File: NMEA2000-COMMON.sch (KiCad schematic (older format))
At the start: 67 parts, among them J2 CAN, Q1 BSS138, Q2 BSS138, SW1 PRG, SW2 INSTANCE, SW3 BUS, U1 MCP2551-I-P, U101 74HC165, U2 TMR-2-2411, U3 74HCT595, U4 74HCT595, U5 Teensy_4.0

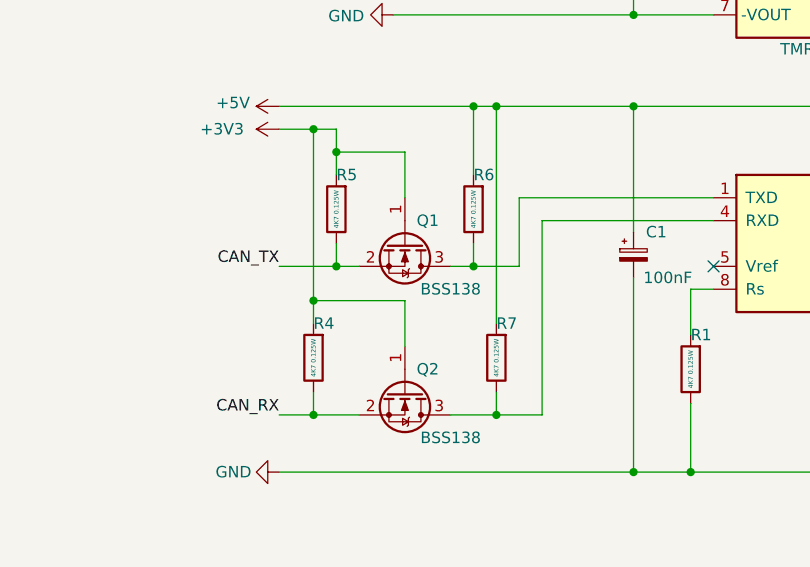
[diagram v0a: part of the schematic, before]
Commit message: Revise logic shifter R values
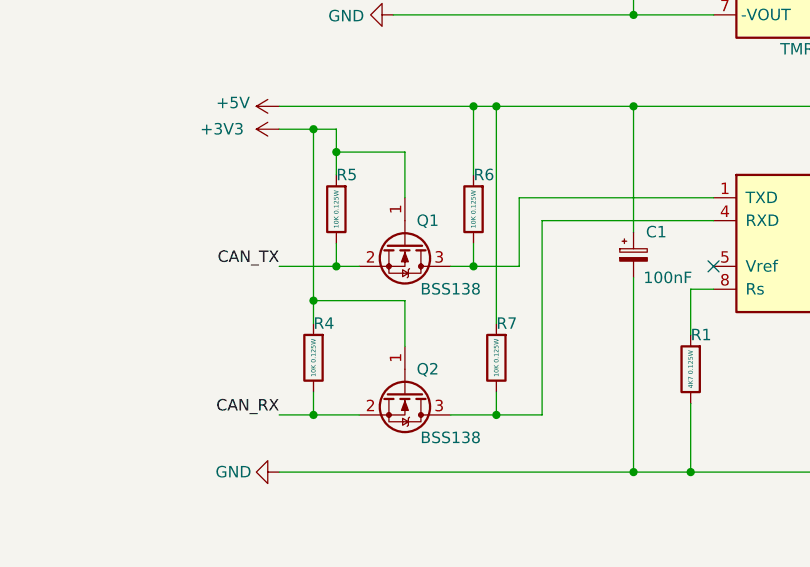
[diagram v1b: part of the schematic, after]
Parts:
- R4, R5, R6, R7: value 4K7 0.125W -> 10K 0.125W
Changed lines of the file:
@@
 P 1500 2200
 F 0 "R5" H 1500 2050 50  0000 R CNN
-F 1 "4K7 0.125W" V 1500 2200 20  0000 C CNN
+F 1 "10K 0.125W" V 1500 2200 20  0000 C CNN
 F 2 "Resistor_SMD:R_0805_2012Metric" V 1430 2200 50  0001 C CNN
 F 3 "~" H 1500 2200 50  0001 C CNN
@@
 P 2100 2200
 F 0 "R6" H 2100 2050 50  0000 R CNN
-F 1 "4K7 0.125W" V 2100 2200 20  0000 C CNN
+F 1 "10K 0.125W" V 2100 2200 20  0000 C CNN
 F 2 "Resistor_SMD:R_0805_2012Metric" V 2030 2200 50  0001 C CNN
 F 3 "~" H 2100 2200 50  0001 C CNN
@@
 P 1400 2850
 F 0 "R4" H 1400 2700 50  0000 R CNN
-F 1 "4K7 0.125W" V 1400 2850 20  0000 C CNN
+F 1 "10K 0.125W" V 1400 2850 20  0000 C CNN
 F 2 "Resistor_SMD:R_0805_2012Metric" V 1330 2850 50  0001 C CNN
 F 3 "~" H 1400 2850 50  0001 C CNN
@@
 P 2200 2850
 F 0 "R7" H 2200 2700 50  0000 R CNN
-F 1 "4K7 0.125W" V 2200 2850 20  0000 C CNN
+F 1 "10K 0.125W" V 2200 2850 20  0000 C CNN
 F 2 "Resistor_SMD:R_0805_2012Metric" V 2130 2850 50  0001 C CNN
 F 3 "~" H 2200 2850 50  0001 C CNN
@@
 Connection ~ 2800 3350
 $Comp
-L power:+3V3 #PWR?
+L power:+3V3 #PWR0105
 U 1 1 639764A6
 P 8150 850
-F 0 "#PWR?" H 8150 700 50  0001 C CNN
+F 0 "#PWR0105" H 8150 700 50  0001 C CNN
 F 1 "+3V3" V 8150 1100 50  0000 C CNN
 F 2 "" H 8150 850 50  0001 C CNN

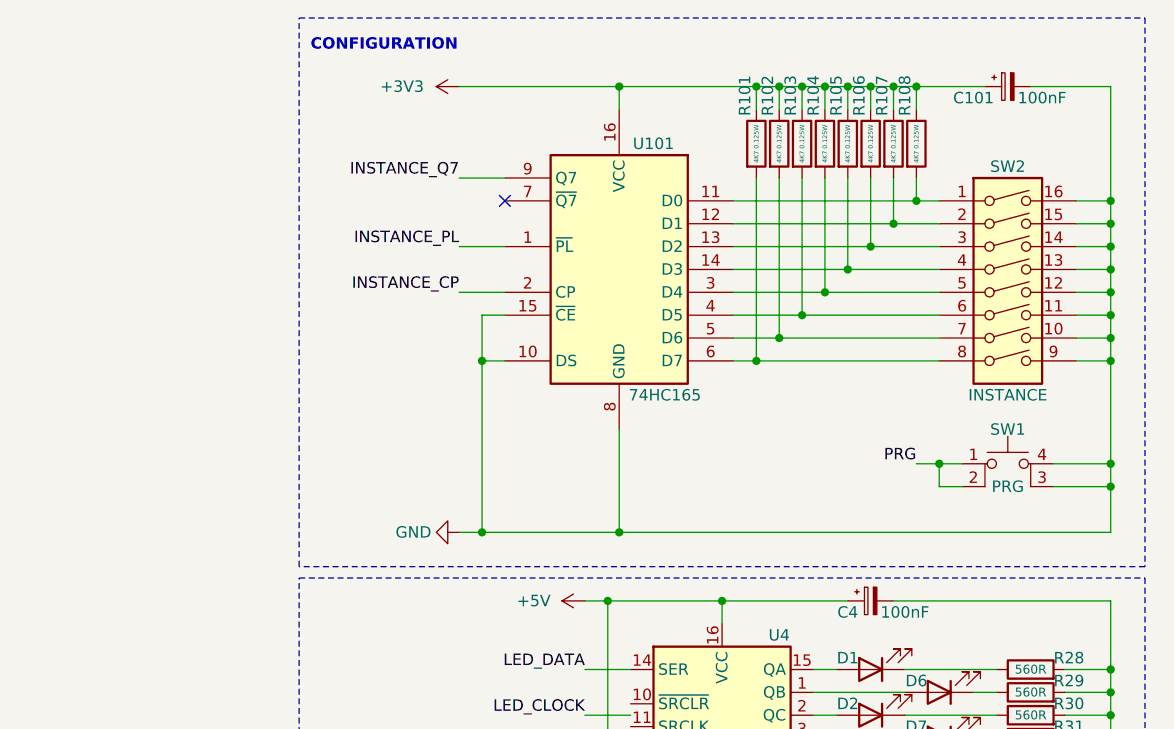
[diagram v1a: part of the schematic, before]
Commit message: Move PISO to 3.3VDC
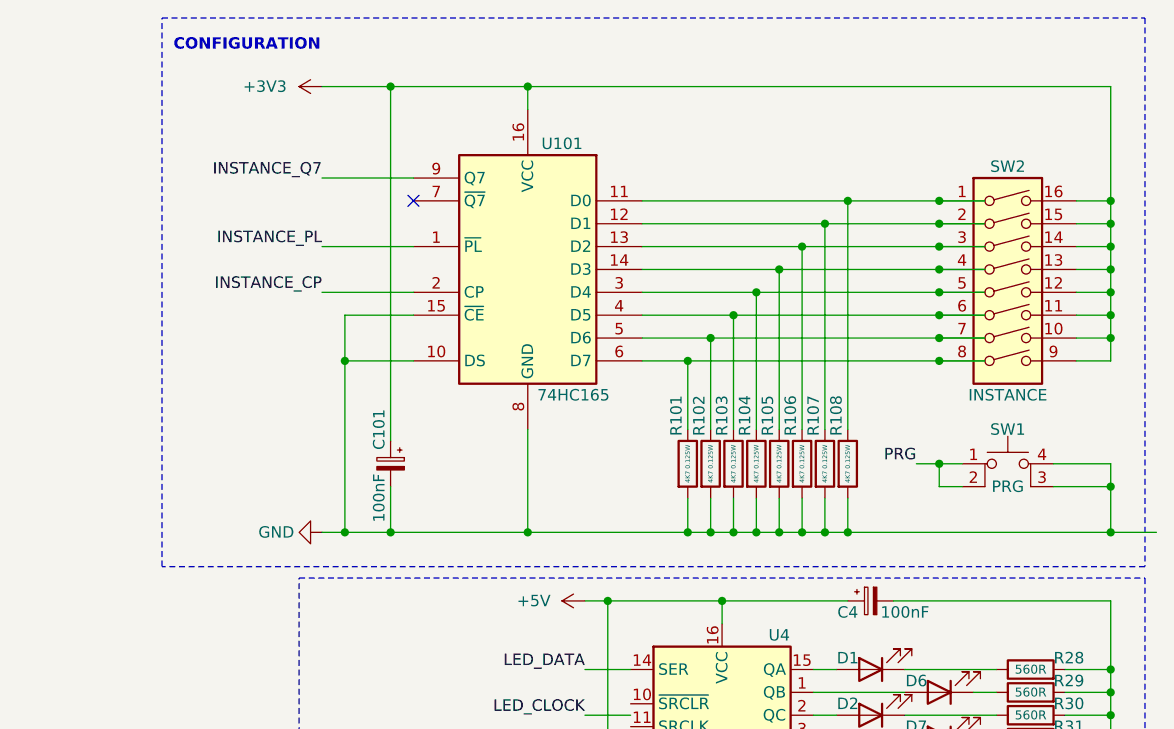
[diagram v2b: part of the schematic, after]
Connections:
- wire segments 266 -> 277
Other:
- moved on the sheet: C101, R101, R102, R103, R104, R105, R106, R107, R108, U101

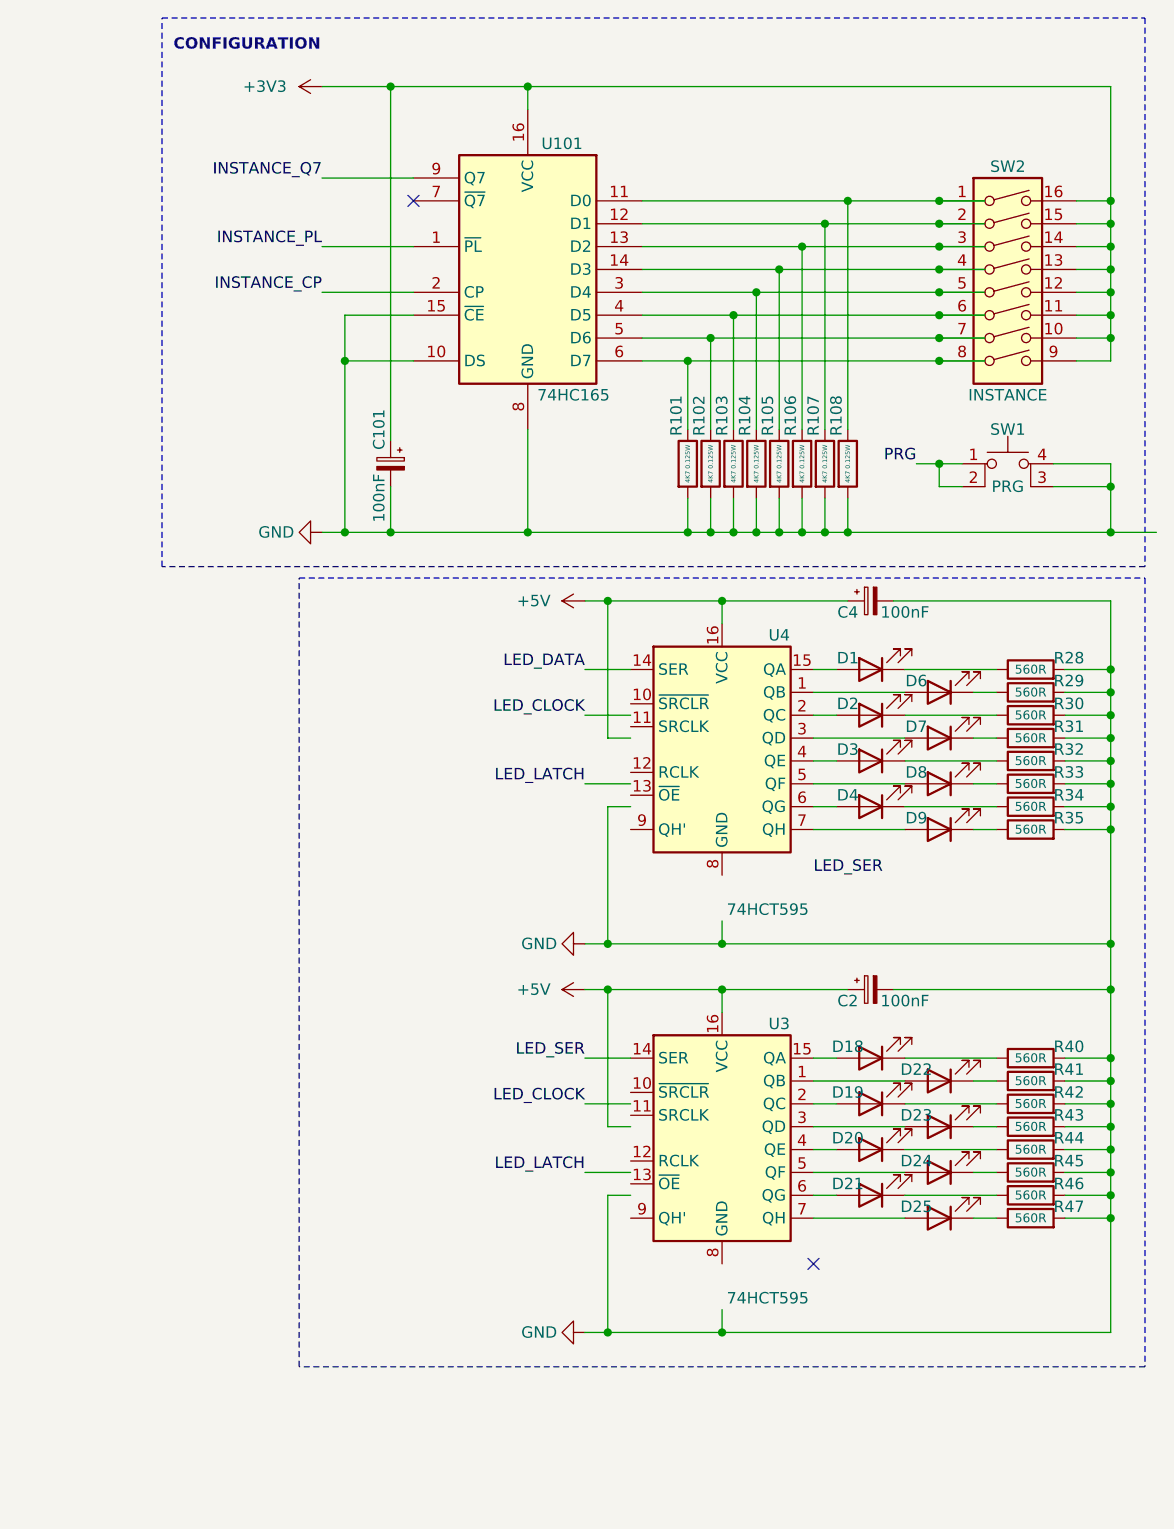
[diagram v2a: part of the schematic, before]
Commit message: Schematic tidy up
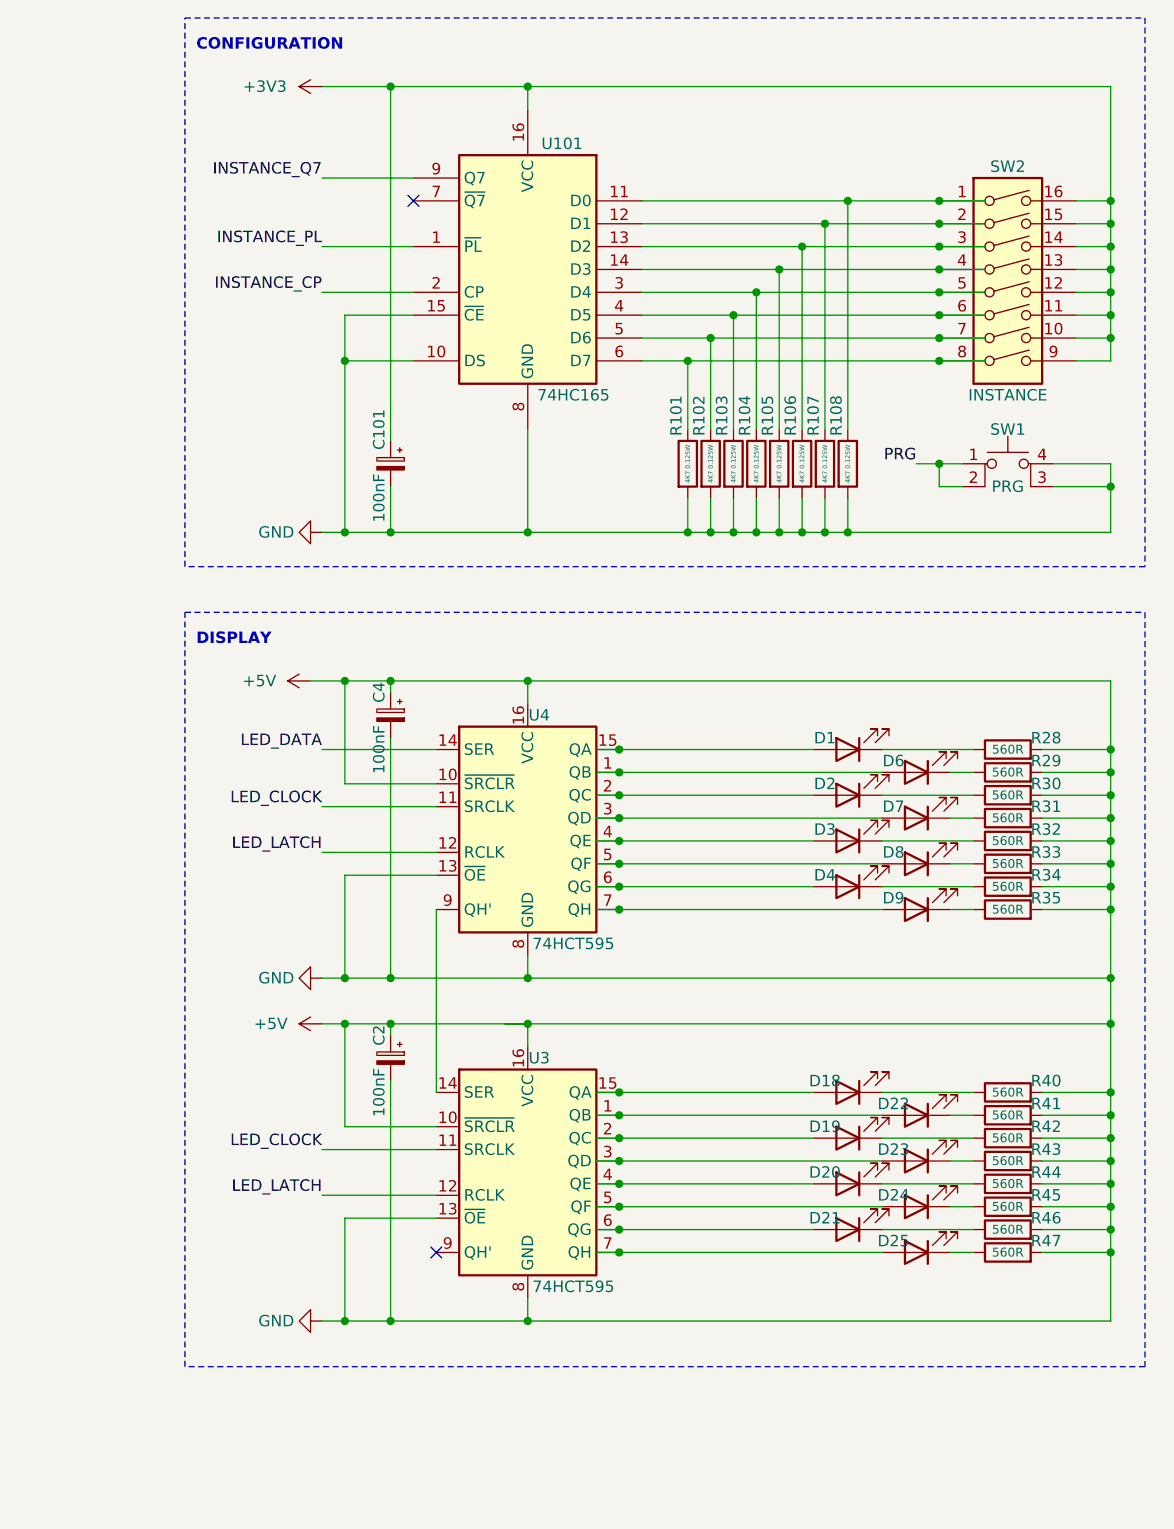
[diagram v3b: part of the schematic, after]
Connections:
- net labels removed: LED_SER
- wire segments 277 -> 299
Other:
- note added: "DISPLAY"
- moved on the sheet: C2, C4, D1, D18, D19, D2, D20, D21, D22, D23, D24, D25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

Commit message: Relay PCB
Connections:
- wire segments 299 -> 275
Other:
- moved on the sheet: C1, C5, F1, J2, Q1, Q2, R1, R2, R4, R5, R6, R7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
